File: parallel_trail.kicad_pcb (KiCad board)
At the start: 2 copper layers, 91 parts, among them U1 TL074, U2 PT2257, U3 TL074, U4 X9C103, U5 X9C103

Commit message: all new
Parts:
- removed ? (x43): , 
- removed the REF** at (121.6, 113.7)
- removed U2: PT2257, Package_DIP:DIP-8_W7.62mm_LongPads
- removed U4, U5: X9C103, Package_DIP:DIP-8_W7.62mm_LongPads
- added C20: 100nf, Capacitor_SMD:C_0805_2012Metric, F.Cu at (82.7, 106.7)
- added C21: 10uF, Capacitor_SMD:C_Elec_4x5.4, F.Cu at (82.3, 111.5)
- added C22: 10uF, Capacitor_SMD:C_Elec_4x5.4, F.Cu at (82.8, 117.3)
- added C23: 10uF, Capacitor_SMD:C_Elec_4x5.4, F.Cu at (74.5, 88.6)
- added C24: 10uF, Capacitor_SMD:C_Elec_4x5.4, F.Cu at (74.5, 94.3)
- added C25: 10uF, Capacitor_SMD:C_Elec_4x5.4, F.Cu at (74.5, 100.1)
- added C26: 10uF, Capacitor_SMD:C_Elec_4x5.4, F.Cu at (74.5, 105.8)
- added C27: 10uF, Capacitor_SMD:C_Elec_4x5.4, F.Cu at (99.5, 99.8)
- added C28: 10uF, Capacitor_SMD:C_Elec_4x5.4, F.Cu at (99.5, 105.5)
- added C29: 150pf, Capacitor_SMD:C_0805_2012Metric, F.Cu at (65.3, 111.8)
- added C30: 10uF, Capacitor_SMD:C_Elec_4x5.4, F.Cu at (74.5, 111.6)
- added C31: 10uF, Capacitor_SMD:C_Elec_4x5.4, F.Cu at (74.5, 117.3)
- added C32: 10uF, Capacitor_SMD:C_Elec_4x5.4, F.Cu at (99.5, 111.3)
- added C33: 10uF, Capacitor_SMD:C_Elec_4x5.4, F.Cu at (99.5, 117.0)
- added C34: 150pf, Capacitor_SMD:C_0805_2012Metric, F.Cu at (58.7, 116.4)
- added R24: 10k, Resistor_SMD:R_0805_2012Metric, F.Cu at (68.6, 111.8)
- added R25: 4.7k, Resistor_SMD:R_0805_2012Metric, F.Cu at (68.6, 101.9)
- added R26: 1M, Resistor_SMD:R_0805_2012Metric, F.Cu at (64.5, 96.6)
- added R27: 1M, Resistor_SMD:R_0805_2012Metric, F.Cu at (52.3, 96.5)
- added R28: 10k, Resistor_SMD:R_0805_2012Metric, F.Cu at (120.2, 111.8)
- added R29: 10k, Resistor_SMD:R_0805_2012Metric, F.Cu at (126.2, 96.6)
- added R30: 4.7k, Resistor_SMD:R_0805_2012Metric, F.Cu at (65.3, 116.3)
- added R31: 10k, Resistor_SMD:R_0805_2012Metric, F.Cu at (62.0, 116.3)
- added R32: 100k, Resistor_SMD:R_0805_2012Metric, F.Cu at (93.7, 105.4)
- added R33: 100k, Resistor_SMD:R_0805_2012Metric, F.Cu at (93.7, 111.3)
- added R34: 100k, Resistor_SMD:R_0805_2012Metric, F.Cu at (93.7, 117.1)
- added R35: 100k, Resistor_SMD:R_0805_2012Metric, F.Cu at (93.7, 88.3)
- added R36: 100k, Resistor_SMD:R_0805_2012Metric, F.Cu at (93.7, 94.1)
- added R37: 100k, Resistor_SMD:R_0805_2012Metric, F.Cu at (93.7, 100.0)
- added REF**: PinHeader_2x08_P2.54mm_Vertical, Connector_PinHeader_2.54mm:PinHeader_2x08_P2.54mm_Vertical, F.Cu at (81.3, 128.8)
- added U6: PT2258, Package_SO:SOP-20_7.5x12.8mm_P1.27mm, F.Cu at (85.1, 96.1)
- C1, C2: footprint Capacitor_THT:C_Rect_L10.0mm_W4.0mm_P7.50mm_MKS4 -> Capacitor_SMD:C_0805_2012Metric
- C10: value 47uf -> 10uF; footprint Capacitor_THT:CP_Radial_D8.0mm_P3.80mm -> Capacitor_SMD:C_Elec_4x5.4
- C11, C7: value 220N -> 220nF; footprint Capacitor_THT:C_Rect_L10.0mm_W4.0mm_P7.50mm_MKS4 -> Capacitor_SMD:C_0805_2012Metric
- C12, C13, C16, C17, C18, C19, C3, C4, C5, C6, C9: footprint Capacitor_THT:CP_Radial_D8.0mm_P3.80mm -> Capacitor_SMD:C_Elec_4x5.4
- C14, C15: footprint Capacitor_THT:C_Disc_D5.0mm_W2.5mm_P2.50mm -> Capacitor_SMD:C_0805_2012Metric
- C8: value 100nf -> 10uF; footprint Capacitor_THT:C_Rect_L10.0mm_W4.0mm_P7.50mm_MKS4 -> Capacitor_SMD:C_Elec_4x5.4
- R1, R10, R11, R12, R13, R16, R17, R18, R19, R2, R20, R21, R22, R23, R3, R4, R5, R6, R7, R8, R9: footprint Resistor_THT:R_Axial_DIN0207_L6.3mm_D2.5mm_P10.16mm_Horizontal -> Resistor_SMD:R_0805_2012Metric
- R14, R15: value 33k -> 4.7k; footprint Resistor_THT:R_Axial_DIN0207_L6.3mm_D2.5mm_P10.16mm_Horizontal -> Resistor_SMD:R_0805_2012Metric
- U1, U3: footprint Package_DIP:DIP-14_W7.62mm_LongPads -> Package_SO:SO-14_3.9x8.65mm_P1.27mm
- moved R8 120.1 mm to (55.4, 96.6), turned to -90 degrees
- moved R7 116.2 mm to (58.4, 96.6), turned to -90 degrees
- moved R9 112.1 mm to (58.9, 88.6)
- moved R6 111.9 mm to (61.5, 96.6), turned to 90 degrees
- moved C9 111.5 mm to (53.6, 90.2)
- moved C4 103.4 mm to (51.8, 105.7), turned to 180 degrees
- moved C3 100.7 mm to (51.8, 114.0)
- moved U1 97.2 mm to (60.5, 104.4), turned to 90 degrees
- moved R3 89.2 mm to (52.3, 100.6), turned to 90 degrees
- moved C2 87.0 mm to (58.7, 111.8), turned to -90 degrees
- moved C6 81.1 mm to (66.0, 88.6), turned to 0 degrees
- moved R2 81.1 mm to (62.0, 111.8), turned to -90 degrees
- moved R4 79.8 mm to (83.3, 86.0), turned to 90 degrees
- moved R1 78.1 mm to (68.6, 116.4), turned to -90 degrees
- moved C1 77.5 mm to (68.6, 106.5), turned to -90 degrees
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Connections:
- net output_buffer_out_left renamed buffer_left_vol_in
- net output_buffer_out_left_inverted renamed buffer_left_vol_in_inverted
- net output_buffer_out_right renamed buffer_right_vol_in
- net output_buffer_out_right_inverted renamed buffer_right_vol_in_inverted
- C10 pad 1: +9V -> Net-(U6-OUT2)
- C10 pad 2: GND -> parallel_vol_1_out
- C3 pad 1: Net-(U1A--) -> Net-(C3-Pad1)
- C4 pad 1: Net-(U1A--) -> Net-(C3-Pad1)
- C4 pad 2: Net-(C4-Pad2) -> parallel_vol_1_in
- C5 pad 1: Net-(U2-OUT-L) -> parallel_vol_2_out
- C6 pad 1: Net-(U1B--) -> Net-(C29-Pad1)
- C6 pad 2: Net-(U2-IN-L) -> parallel_vol_2_in
- C8 pad 1: GND -> Net-(U6-OUT1)
- C8 pad 2: +9V -> parallel_vol_2_out
- R5 pad 2: Net-(C4-Pad2) -> parallel_vol_1_out
- U1 pad 1: Net-(U1A--) -> Net-(C3-Pad1)
- U1 pad 7: Net-(U1B--) -> Net-(C29-Pad1)
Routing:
- net GND: track 65.6 -> 378.9 mm, vias 0 -> 2
- net mcp2_A2: track 103.2 -> 0.00 mm
- net mcp2_A0: track 97.4 -> 0.00 mm
- net parallel_send_1: track 151.7 -> 56.7 mm
- net mcp2_A1: track 93.7 -> 0.00 mm
- net buffer_left_vol_in_inverted: track 155.1 -> 74.6 mm, vias 0 -> 2
- net Net-(C14-Pad1): track 93.9 -> 21.9 mm, vias 0 -> 2
- net -9V: track 159.4 -> 87.5 mm, vias 0 -> 3
- net mcp2_A3: track 70.5 -> 0.00 mm
- net mcp2_A4: track 63.0 -> 0.00 mm
- net Net-(C4-Pad2): track 52.1 -> 0.00 mm
- net mcp2_A5: track 47.2 -> 0.00 mm
- net parallel_vol_1_out: track 0.00 -> 43.6 mm
- net +9V: track 164.0 -> 121.7 mm, vias 0 -> 3
- net parallel_vol_1_in: track 0.00 -> 38.3 mm
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- removed copper zone on F.Cu, net GND
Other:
- board outline added: 90 x 50 mm
- board text added: "+9v"
- board text added: "-9v"
- board text added: "B_IN_L"
- board text added: "B_IN_R"
- board text added: "B_OUT_L"
- board text added: "B_OUT_L_I"
- board text added: "B_OUT_R"
- board text added: "B_OUT_R_I"
- board text added: "GND"
- board text added: "NC"
- board text added: "PM_IN"
- board text added: "PM_OUT"
- board text added: "PR1"
- board text added: "PS1"
- board text added: "SCL"
- board text added: "SDA"

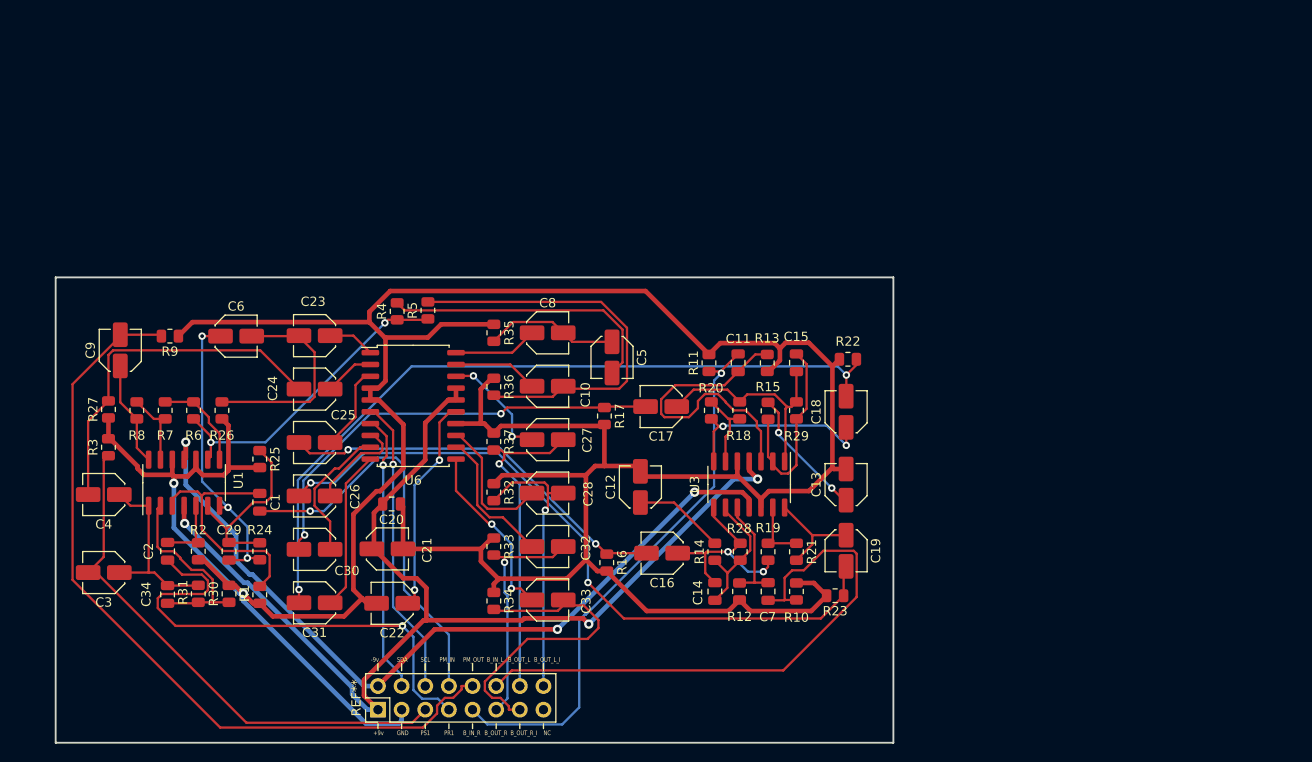
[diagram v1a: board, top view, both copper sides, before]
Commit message: added phase switch and rerouted
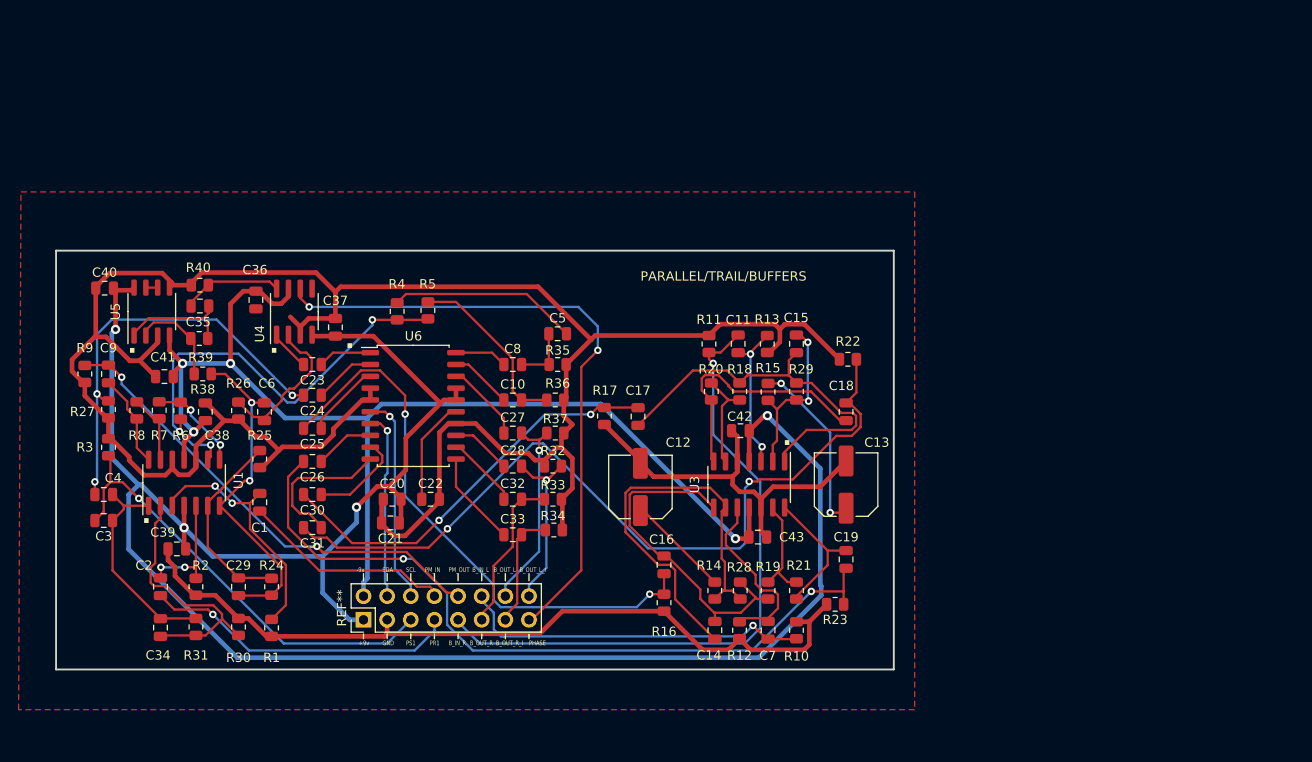
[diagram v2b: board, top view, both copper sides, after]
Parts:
- added C35: 10uF, Capacitor_SMD:C_0805_2012Metric, F.Cu at (62.1, 85.4)
- added C36: 100nf, Capacitor_SMD:C_0805_2012Metric, F.Cu at (68.2, 84.8)
- added C37: 100nf, Capacitor_SMD:C_0805_2012Metric, F.Cu at (76.7, 87.7)
- added C38: 100nf, Capacitor_SMD:C_0805_2012Metric, F.Cu at (62.7, 96.8)
- added C39: 100nf, Capacitor_SMD:C_0805_2012Metric, F.Cu at (59.7, 111.5)
- added C40: 100nf, Capacitor_SMD:C_0805_2012Metric, F.Cu at (51.9, 83.5)
- added C41: 100nf, Capacitor_SMD:C_0805_2012Metric, F.Cu at (58.3, 93.0)
- added C42: 100nf, Capacitor_SMD:C_0805_2012Metric, F.Cu at (120.2, 98.8)
- added C43: 100nf, Capacitor_SMD:C_0805_2012Metric, F.Cu at (122.1, 110.2)
- added R38: 10k, Resistor_SMD:R_0805_2012Metric, F.Cu at (62.5, 92.7)
- added R39: 10k, Resistor_SMD:R_0805_2012Metric, F.Cu at (62.1, 88.9)
- added R40: 1M, Resistor_SMD:R_0805_2012Metric, F.Cu at (62.1, 83.2)
- added U4: DG419LDY, Package_SO:SOIC-8_3.9x4.9mm_P1.27mm, F.Cu at (72.3, 86.0)
- added U5: TL072, Package_SO:SO-8_3.9x4.9mm_P1.27mm, F.Cu at (57.0, 86.0)
- C10, C16, C17, C18, C19, C21, C22, C23, C24, C25, C26, C27, C28, C3, C30, C31, C32, C33, C4, C5, C6, C8, C9: footprint Capacitor_SMD:C_Elec_4x5.4 -> Capacitor_SMD:C_0805_2012Metric
- C12, C13: footprint Capacitor_SMD:C_Elec_4x5.4 -> Capacitor_SMD:C_Elec_6.3x5.4
- moved C22 11.9 mm to (86.9, 106.2), turned to 0 degrees
- moved R9 10.0 mm to (49.8, 92.7), turned to 90 degrees
- moved R34 9.99 mm to (100.2, 109.5), turned to 180 degrees
- moved REF** 9.78 mm to (79.7, 119.1)
- moved C6 8.68 mm to (69.1, 96.8), turned to -90 degrees
- moved R33 8.13 mm to (100.1, 106.2), turned to 180 degrees
- moved C31 8.08 mm to (74.2, 109.2)
- moved C33 7.95 mm to (95.8, 110.0)
- moved R35 7.66 mm to (100.6, 91.7), turned to 180 degrees
- moved R16 7.51 mm to (112.0, 117.3)
- moved R32 6.94 mm to (100.1, 102.6), turned to 0 degrees
- moved R36 6.76 mm to (100.3, 95.5), turned to 180 degrees
- moved R37 6.67 mm to (100.3, 99.1), turned to 180 degrees
- moved C5 6.37 mm to (100.6, 88.4), turned to 0 degrees
- moved C32 6.31 mm to (95.8, 106.2)
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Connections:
- C6 pad 2: parallel_vol_2_in -> Net-(C6-Pad2)
- R26 pad 2: parallel_vol_2_in -> Net-(C6-Pad2)
- REF** pad 15: (no net) -> parallel_phase
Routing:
- net +9V: track 121.7 -> 225.8 mm, vias 3 -> 4
- net parallel_phase: track 0.00 -> 69.0 mm, vias 0 -> 2
- net -9V: track 87.5 -> 125.9 mm, vias 3 -> 4
- net parallel_mixer_out: track 85.2 -> 50.8 mm, vias 0 -> 2
- net Net-(U3C--): track 14.6 -> 45.3 mm
- net parallel_vol_1_out: track 43.6 -> 19.2 mm
- net output_buffer_in_left: track 61.9 -> 38.0 mm, vias 0 -> 1
- net output_buffer_out_right_inverted: track 34.0 -> 12.6 mm
- net parallel_mixer_in: track 43.9 -> 22.9 mm, vias 1 -> 0
- net buffer_left_vol_in: track 42.8 -> 62.0 mm
- net parallel_return_1: track 52.2 -> 33.9 mm
- net parallel_vol_2_in: track 22.5 -> 4.45 mm
- net Net-(C15-Pad1): track 24.5 -> 42.2 mm
- net Net-(C6-Pad2): track 0.00 -> 16.6 mm
- net Net-(U3A-+): track 32.6 -> 16.2 mm, vias 0 -> 2
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- added copper zone on F.Cu, net GND
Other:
- board size 90 x 50 mm -> 90 x 45 mm
- board text added: "."
- board text added: "PARALLEL/TRAIL/BUFFERS"
- board text added: "PHASE"
- board text removed: "NC"
